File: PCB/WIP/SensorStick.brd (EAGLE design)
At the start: 59.7 x 72.1 mm, 89 parts, among them U1 TPD4F003DQDR, U10 LIS3MDLTR, U11 LIS3MDLTR, U2 BMI088, U3 BMI088, U4 BMI088, U5 STM32H743ZIT6, U9 LIS3MDLTR, Y1 ECS-TXO-3225MV-400-TR

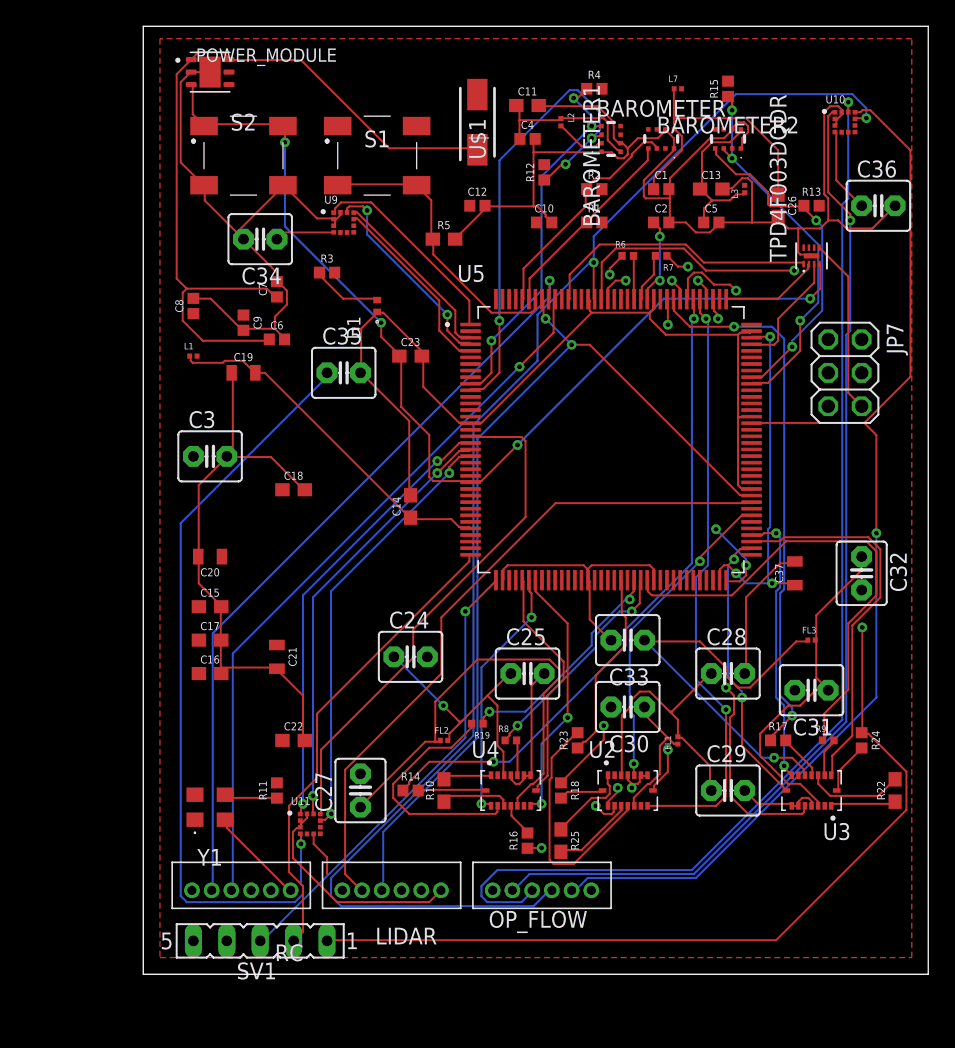
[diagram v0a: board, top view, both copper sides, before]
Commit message: a lot less airewires but still airwires
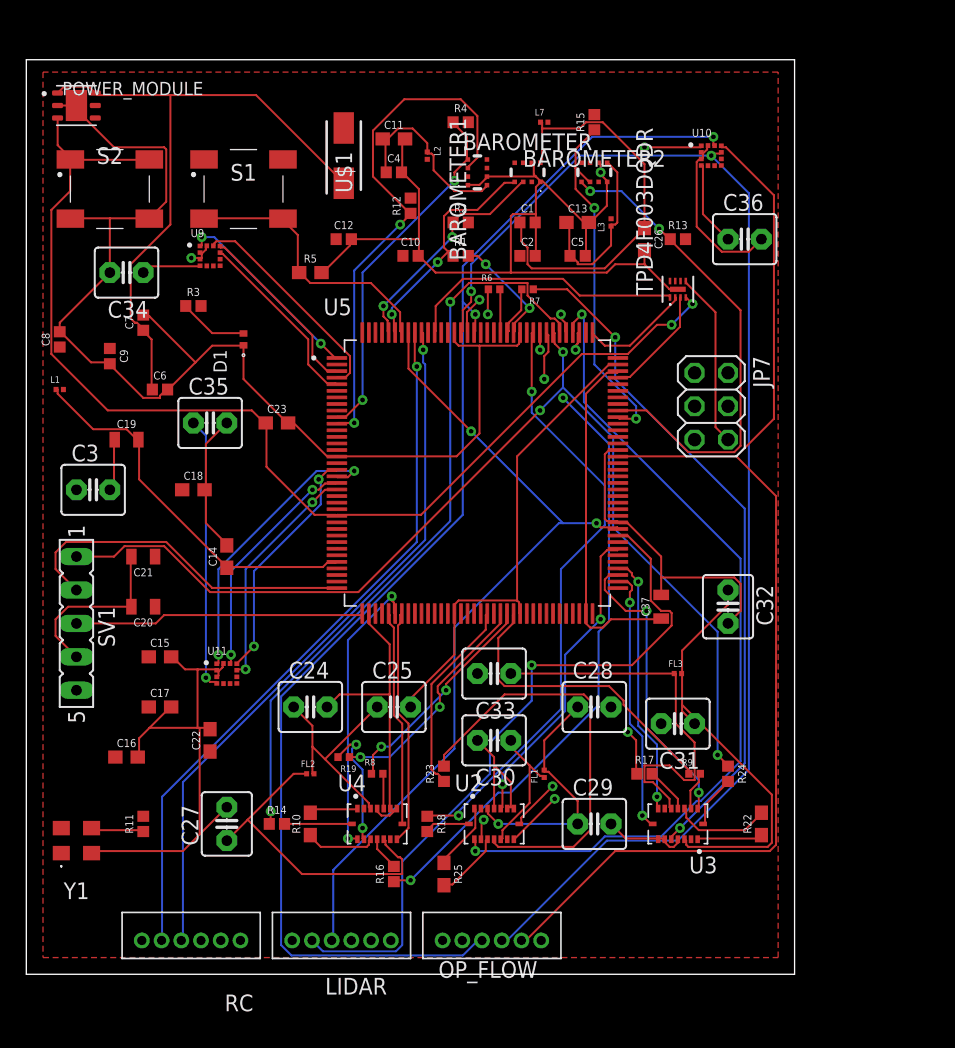
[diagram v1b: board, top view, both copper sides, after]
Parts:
- moved SV1 27.9 mm to (3.81, 26.7), turned to 270 degrees
- moved C14 14.5 mm to (15.2, 31.8)
- moved U11 13.1 mm to (15.2, 22.9)
- moved C21 12.7 mm to (8.89, 31.8), turned to 180 degrees
- moved C23 11.4 mm to (19.1, 41.9)
- moved C35 10.9 mm to (14.0, 41.9)
- moved BAROMETER1 10.5 mm to (34.3, 61.0)
- moved BAROMETER2 10.5 mm to (43.2, 61.0)
- moved C13 10.5 mm to (41.9, 57.1)
- moved C28 10.5 mm to (43.2, 20.3)
- moved C29 10.5 mm to (43.2, 11.4)
- moved C37 10.5 mm to (48.3, 27.9)
- moved C5 10.5 mm to (41.9, 54.6)
- moved FL1 10.5 mm to (39.4, 15.2)
- moved L7 10.5 mm to (39.4, 64.8)
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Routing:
- net N$7: track 58.8 -> 20.8 mm
- net SPI6_SCK: track 102.6 -> 75.6 mm
- net SPI5_CS: track 39.2 -> 18.4 mm, vias 0 -> 2
- net SPI3_MISO: track 44.4 -> 64.5 mm
- net GND: track 330.3 -> 348.3 mm, vias 1 -> 2
- net GPIO_EXTI1: track 99.4 -> 83.7 mm, vias 2 -> 3
- net SPI5_MOSI: track 33.1 -> 17.8 mm
- net SPI5_MISO: track 33.1 -> 17.9 mm
- net EXTI0_1: track 18.8 -> 32.1 mm
- net N$17: track 36.5 -> 23.3 mm
- net USART2_RX: track 35.0 -> 22.1 mm, vias 1 -> 0
- net SPI5_SCK: track 34.3 -> 22.2 mm
- net I2C3_SCL: track 25.6 -> 37.4 mm
- net 3V3: track 20.4 -> 8.78 mm, vias 4 -> 2
- net 5V: track 60.5 -> 49.5 mm
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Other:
- board size 59.7 x 72.1 mm -> 58.4 x 69.5 mm

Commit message: first draft pretty much
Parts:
- removed JP7: (no value), pinhead:2X03
- C24, C25, C27, C28, C29, C30, C31, C32, C33: value 0.1uf -> 0.1uF; device capacitor-wima:C2.5-4 -> SparkFun-Capacitors:0603
- C3, C34, C35, C36: device capacitor-wima:C2.5-4 -> SparkFun-Capacitors:0603
- moved C3 33.0 mm to (3.81, 3.81), turned to 180 degrees
- moved C32 24.5 mm to (44.5, 5.08), turned to 0 degrees
- moved C35 15.2 mm to (14.0, 26.7)
- moved C36 10.8 mm to (47.0, 63.5)
- moved C29 10.2 mm to (43.2, 21.6)
- moved R24 9.92 mm to (47.0, 22.9)
- moved R16 9.25 mm to (19.1, 10.2), turned to 270 degrees
- moved C28 8.52 mm to (35.6, 16.5)
- moved R22 8.03 mm to (48.3, 8.89)
- moved C18 7.73 mm to (5.08, 35.6)
- moved R9 6.48 mm to (44.5, 16.5)
- moved R18 6.35 mm to (30.5, 17.8)
- moved U3 5.68 mm to (44.5, 8.89)
- moved C14 5.39 mm to (11.4, 35.6), turned to 180 degrees
- moved R17 5.24 mm to (41.9, 16.5)
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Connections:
- removed net SWCLK_O1: JP7.3
- removed net SWDIO_O1: JP7.5
- removed net SWO_O1: JP7.1
- removed net USART1_RX: JP7.4
- removed net USART1_TX: JP7.2
- net 3V2: now also C28.2, C29.2; no longer C28.1, C29.1
- net 3V3: now also C3.2; no longer C3.1
- net 3V4: now also C24.2, C25.2; no longer C24.1, C25.1
- net 3V5: now also C31.2, C32.2; no longer C31.1, C32.1
- net GND: now also C24.1, C25.1, C27.1, C28.1, C29.1, C3.1, C30.1, C31.1, C32.1, C33.1, C34.1, C35.1, C36.1; no longer C24.2, C25.2, C27.2, C28.2, C29.2, C3.2, C30.2, C31.2, C32.2, C33.2, C34.2, C35.2, C36.2
- net N$10: now also C33.2; no longer C33.1
- net N$11: now also C36.2; no longer C36.1
- net N$4: now also C34.2; no longer C34.1
- net N$7: now also C35.2; no longer C35.1
- net N$8: now also C27.2; no longer C27.1
- net N$9: now also C30.2; no longer C30.1
- net NRST_O: no longer JP7.6
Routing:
- net 3V3: track 8.78 -> 263.0 mm, vias 2 -> 18
- net GND: track 348.3 -> 288.0 mm, vias 2 -> 23
- net SPI6_SCK: track 75.6 -> 108.6 mm, vias 2 -> 3
- net I2C2_SCL: track 27.5 -> 58.8 mm, vias 2 -> 0
- net SPI3_MOSI: track 44.9 -> 73.6 mm, vias 2 -> 4
- net I2C4_SDA: track 62.9 -> 91.2 mm, vias 2 -> 3
- net CSB_ACCEL3: track 42.2 -> 65.3 mm
- net SPI2_SCK: track 20.2 -> 43.2 mm
- net GPIO_EXTI2: track 52.1 -> 69.6 mm, vias 3 -> 2
- net N$14: track 3.79 -> 19.3 mm, vias 0 -> 2
- net UART5_RX: track 54.0 -> 68.2 mm
- net EXTI0_1: track 32.1 -> 18.1 mm
- net UART5_TX: track 54.3 -> 68.3 mm
- net I2C2_SDA: track 40.3 -> 26.3 mm
- net 3V5: track 32.5 -> 19.0 mm
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- added copper zone on layer 15, net 3V3
- removed copper zone on layer 1, net 3V3
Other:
- board size 58.4 x 69.5 mm -> 54.6 x 67 mm

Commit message: slight changes but this is rough draft 1 officially
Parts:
- removed R10, R22, R25: 0, SparkFun-Resistors:0603
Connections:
- removed net IMU_INT1: R22.1, U3.1
- removed net IMU_INT2: R10.2, U4.1
- removed net IMU_INT4: R10.1, U4.13
- removed net IMU_INT5: R25.1, U2.1
- removed net IMU_INT6: R25.2, U2.13
- removed net JTDI: U5.110
- removed net LPUART1_RX: U5.102
- removed net LPUART1_TX: U5.101
- removed net N$18: RC.4
- removed net N$21: LIDAR.5
- removed net N$22: LIDAR.4
- removed net SPI2_CS: U5.73
- removed net SPI3_CS: U5.40
- removed net UART4_RX: U5.35
- removed net UART4_TX: U5.34
- removed net UART8_RX: U5.141
- removed net UART8_TX: U5.142
- new net GPIO1: LIDAR.4, U5.57
- new net N$20: U4.1, U4.13
- new net N$23: U2.1, U2.13
- new net XSHUT: LIDAR.5, U5.27
- net GND: no longer RC.6
- net IMU_INT3: now also U3.1; no longer R22.2
- net N$19: now also RC.6; no longer RC.5
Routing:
- net XSHUT: track 0.00 -> 38.4 mm, vias 0 -> 1
- net GPIO1: track 0.00 -> 28.7 mm, vias 0 -> 4
- net IMU_INT6: track 5.69 -> 0.00 mm
- net IMU_INT4: track 5.43 -> 0.00 mm
- net IMU_INT2: track 3.76 -> 0.00 mm
- net IMU_INT5: track 3.76 -> 0.00 mm
- net N$23: track 0.00 -> 3.42 mm
- net N$20: track 0.00 -> 3.04 mm
- net IMU_INT1: track 2.49 -> 0.00 mm
- net GND: track 288.0 -> 289.5 mm
- net IMU_INT3: track 3.83 -> 3.11 mm

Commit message: cleaned up layout
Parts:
- removed L1: BLM03AG601SN1D, BLM03AG601SN1D:BEADC0603X33N
- added C38, C39: 1.0uF, SparkFun-Capacitors:0805
- added CON1: B4B-ZR, jst:B4B-ZR
- added JP1: (no value), pinhead:2X03
- added RADIO: B6B-ZR, jst:B6B-ZR
- C14: value 0.1uF -> 1.0uF; device SparkFun-Capacitors:0603 -> SparkFun-Capacitors:0805
- moved C19 55.1 mm to (0.00, -15.2)
- moved C14 48.4 mm to (0.00, -11.4), turned to 0 degrees
- moved C8 4.02 mm to (3.81, 50.8)
- renumbered SV1 to GPS
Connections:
- new net DM: CON1.2
- new net DP: CON1.3
- new net GND1: C14.2, C15.2, C16.2, C17.2, C18.2, C20.2, C21.2, C22.2
- new net GND2: C19.2
- new net GND3: C38.2
- new net GND4: C39.2
- new net UART4_RX: JP1.4, U5.103
- new net UART4_TX: JP1.2, U5.104
- new net UART8_RX: RADIO.3, U5.141
- new net UART8_TX: RADIO.2, U5.142
- new net VREF1: C14.1
- new net VREF2: C19.1
- new net VREF3: C38.1
- new net VREF4: C39.1
- net 3V3: now also RADIO.1; no longer C15.1, C16.1, C17.1, C18.1, C20.1, C21.1, C22.1, L1.2
- net 5V_IN: now also CON1.4
- net GND: now also CON1.1; no longer C14.2, C15.2, C16.2, C17.2, C18.2, C19.1, C20.2, C21.2, C22.2
- net N$19: now also RADIO.6
- net NRST_O: now also JP1.6
- net SWCLK_O: now also JP1.3
- net SWDIO_O: now also JP1.5
- net SWO_O: now also JP1.1
- net VREF: now also C15.1, C16.1, C17.1, C18.1, C20.1, C21.1, C22.1; no longer C14.1, C19.2, L1.1
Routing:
- net UART8_RX: track 0.00 -> 51.3 mm, vias 0 -> 1
- net N$19: track 0.00 -> 46.7 mm
- net 3V3: track 263.0 -> 226.9 mm, vias 18 -> 19
- net NRST_O: track 0.00 -> 33.5 mm, vias 0 -> 2
- net UART8_TX: track 0.00 -> 29.4 mm, vias 0 -> 1
- net GPIO_EXTI3: track 34.6 -> 9.73 mm
- net UART4_RX: track 0.00 -> 14.6 mm, vias 0 -> 2
- net UART4_TX: track 0.00 -> 10.3 mm, vias 0 -> 1
- net SWO_O: track 0.00 -> 9.89 mm, vias 0 -> 1
- net I2C3_SDA: track 32.6 -> 41.7 mm
- net GND: track 289.5 -> 298.5 mm, vias 23 -> 22
- net N$10: track 27.1 -> 19.8 mm
- net VREF: track 26.0 -> 32.0 mm
- net I2C3_SCL: track 25.7 -> 28.3 mm, vias 2 -> 4
- net SPI6_CS: track 79.5 -> 81.9 mm
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
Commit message: bypass cap fixes and other minor stuffs
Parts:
- removed CON1: B4B-ZR, jst:B4B-ZR
- removed U11, U9: LIS3MDLTR, LIS3MDLTR:XDCR_LIS3MDLTR
- added C40, C49: 1.0uF, SparkFun-Capacitors:0805
- added C41, C42, C43, C44, C45, C46, C47, C48: 0.1uF, SparkFun-Capacitors:0603
- added C50: 0.1uf, SparkFun-Capacitors:0805
- added C51, C52: 5.6pF, SparkFun-Capacitors:0805
- added J1: 10118192-0001LF, ce-capstone:AMPHENOL_10118192-0001LF
- added R10: 220, ce-capstone:RESC1005X35N
- added U6, U7: LIS3MDLTR, LIS3MDLTR:XDCR_LIS3MDLTR
- added Y2: ABLS-8.000MHZ-B2-T, ce-capstone:XTAL_ABLS-8.000MHZ-B2-T
- C3: value 0.1uF -> 2.2uF; device SparkFun-Capacitors:0603 -> SparkFun-Capacitors:0805
- C34: value 0.1uF -> 1.0uF; device SparkFun-Capacitors:0603 -> SparkFun-Capacitors:0805
- C35: value 0.1uF -> 0.1uf; device SparkFun-Capacitors:0603 -> SparkFun-Capacitors:0805
- C37: value 1.0uF -> 2.2uf
- moved R24 128.6 mm to (-71.1, 73.7), turned to 0 degrees
- moved FL3 127.2 mm to (-64.8, 77.5)
- moved L3 126.3 mm to (-80.0, 77.5), turned to 0 degrees
- moved C28 125.7 mm to (-80.0, 66.0)
- moved OP_FLOW 124.4 mm to (-80.0, 34.3), turned to 0 degrees
- moved C37 120.9 mm to (-67.3, 62.2), turned to 0 degrees
- moved C26 119.9 mm to (-72.4, 66.0), turned to 0 degrees
- moved R17 119.9 mm to (-63.5, 73.7)
- moved R6 116.6 mm to (-78.7, 73.7)
- moved C2 115.5 mm to (-76.2, 69.8)
- moved R23 115.3 mm to (-68.6, 73.7), turned to 0 degrees
- moved C39 113.4 mm to (-74.9, 62.2)
- moved BAROMETER2 113.1 mm to (-69.8, 57.1)
- moved R18 111.5 mm to (-66.0, 73.7), turned to 0 degrees
- moved C1 111.4 mm to (-72.4, 69.8)
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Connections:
- removed net DM: CON1.2
- removed net DP: CON1.3
- removed net N$11: C36.2, U10.4
- removed net N$12: C37.1, U5.106, U5.71
- removed net N$4: C34.2, U9.4
- removed net VREF: C15.1, C16.1, C17.1, C18.1, C20.1, C21.1, C22.1, U5.32
- new net AGND: C3.1, C34.1, C35.1, C37.1, C49.1, C50.1
- new net OSC_OUT: R10.1, U5.24
- new net VBAT: C40.2, U5.6
- new net VCAP: C3.2, C37.2, U5.106, U5.71
- new net VDD: C15.1, C16.1, C17.1, C18.1, C20.1, C21.1, C22.1
- new net VDDA: C34.2, C35.2, U5.33
- new net VREFP: C49.2, C50.2, U5.32
- net 3V3: now also C36.2, C41.2, C42.2, C43.2, C44.2, C45.2, C46.2, C47.2, C48.2, U6.5, U6.6, U7.5, U7.6; no longer C3.2, U11.5, U11.6, U5.33, U5.6, U9.5, U9.6
- net 5V_IN: now also J1.1; no longer CON1.4
- net GND: now also C40.1, C41.1, C42.1, C43.1, C44.1, C45.1, C46.1, C47.1, C48.1, C51.1, C52.1, J1.5, U10.4, U6.12, U6.2, U6.3, U6.4, U7.12, U7.2, U7.3, U7.4; no longer C3.1, C34.1, C35.1, C37.2, CON1.1, U11.12, U11.2, U11.3, U9.12, U9.2, U9.3
- net N$7: now also C52.2, R10.2, Y2.1; no longer C35.2, U11.4
- net OSC_IN: now also C51.2, U5.23, Y2.2
- net SPI4_CS: now also U7.10; no longer U9.10
- net SPI4_MISO: now also U7.11; no longer U9.11
- net SPI4_MOSI: now also U7.9; no longer U9.9
- net SPI4_SCK: now also U7.1; no longer U9.1
- net SPI5_CS: now also U6.10; no longer U11.10
- net SPI5_MISO: now also U6.11; no longer U11.11
- net SPI5_MOSI: now also U6.9; no longer U11.9
- net SPI5_SCK: now also U6.1; no longer U11.1
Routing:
- net GND: track 298.5 -> 0.00 mm, vias 22 -> 0
- net 3V3: track 226.9 -> 0.00 mm, vias 19 -> 0
- net SPI6_SCK: track 108.6 -> 0.00 mm, vias 3 -> 0
- net SPI6_MISO: track 106.4 -> 0.00 mm, vias 2 -> 0
- net SPI6_MOSI: track 97.1 -> 0.00 mm, vias 2 -> 0
- net I2C4_SDA: track 91.2 -> 0.00 mm, vias 3 -> 0
- net SPI6_CS: track 81.9 -> 0.00 mm
- net NRST: track 81.1 -> 0.00 mm, vias 2 -> 0
- net SPI3_MOSI: track 73.6 -> 0.00 mm, vias 4 -> 0
- net GPIO_EXTI1: track 71.5 -> 0.00 mm, vias 3 -> 0
- net GPIO_EXTI2: track 69.6 -> 0.00 mm, vias 2 -> 0
- net UART5_TX: track 68.3 -> 0.00 mm, vias 1 -> 0
- net UART5_RX: track 68.2 -> 0.00 mm, vias 1 -> 0
- net CSB_ACCEL3: track 65.3 -> 0.00 mm, vias 2 -> 0
- net I2C2_SCL: track 58.8 -> 0.00 mm
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- removed copper zone on layer 15, net 3V3
- removed copper zone on layer 2, net GND
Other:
- board size 54.6 x 67 mm -> 160 x 100 mm
